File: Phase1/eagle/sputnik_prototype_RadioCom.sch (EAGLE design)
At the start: 73 parts, among them Y1 32MHz

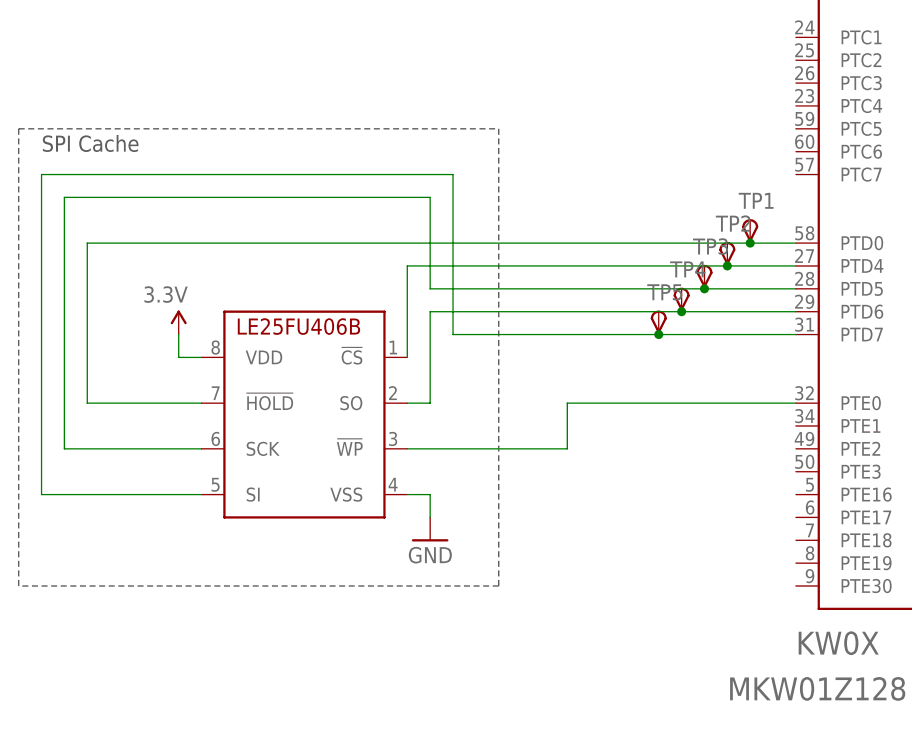
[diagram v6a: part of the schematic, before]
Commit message: Fixed OIs, fixed SysCon LDO, replaced SPI cache
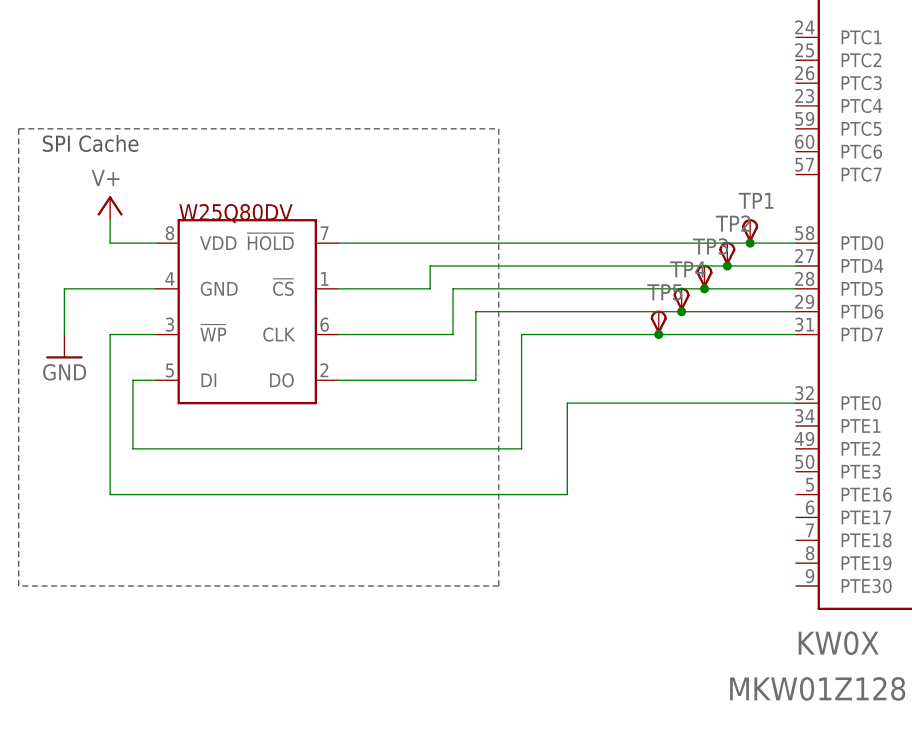
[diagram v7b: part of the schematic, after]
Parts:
- removed CACHE: LE25FU406B, psas_c3_team05:LE25FU406B
- added U$1: W25Q80DV, psas_c3_team05:W25Q80DV
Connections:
- removed net N$4: CACHE.!CS, KW0X.PTD4, TP2.PP
- new net N$28: KW0X.PTD4, TP2.PP, U$1.!CS
- net 3.3V: no longer CACHE.VDD
- net GND: now also U$1.GND; no longer CACHE.VSS
- net N$12: now also U$1.DO; no longer CACHE.SO
- net N$14: now also U$1.CLK; no longer CACHE.SCK
- net N$15: now also U$1.DI; no longer CACHE.SI
- net N$23: now also U$1.!HOLD; no longer CACHE.!HOLD
- net N$26: now also U$1.!WP; no longer CACHE.!WP
- net V+: now also U$1.VDD
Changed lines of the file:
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@@
 <?xml version="1.0" encoding="utf-8"?>
 <!DOCTYPE eagle SYSTEM "eagle.dtd">
-<eagle version="7.3.0">
+<eagle version="7.5.0">
 <drawing>
 <settings>
@@
 <part name="GND41" library="psas_c3_team05" deviceset="GND" device=""/>
 <part name="3.3V2" library="psas_c3_team05" deviceset="V+" device=""/>
-<part name="CACHE" library="psas_c3_team05" deviceset="LE25FU406B" device="">
-<attribute name="DIST" value="Digi-Key"/>
-<attribute name="DPN" value="W25Q80DVSSIG-ND"/>
-<attribute name="MFN" value="Winbond Electronics"/>
-<attribute name="MPN" value="W25Q80DVSSIG"/>
-</part>
 <part name="JP1" library="psas_c3_team05" deviceset="PINHD-1X2" device=""/>
 <part name="GND1" library="psas_c3_team05" deviceset="GND" device=""/>
@@
 <part name="3.3V1" library="psas_c3_team05" deviceset="V+" device=""/>
 <part name="GND34" library="psas_c3_team05" deviceset="GND" device=""/>
-<part name="P+1" library="SparkFun-v5" deviceset="3.3V" device=""/>
 <part name="U$8" library="psas_c3_team05" deviceset="AAT3215" device="">
 <attribute name="MFN" value="Skyworks"/>
@@
 <attribute name="MFN-PN" value="AAT3215"/>
 </part>
+<part name="U$1" library="psas_c3_team05" deviceset="W25Q80DV" device=""/>
+<part name="3.3V4" library="psas_c3_team05" deviceset="V+" device=""/>
 </parts>
 <sheets>
@@
 <instance part="GND41" gate="1" x="452.12" y="304.8"/>
 <instance part="3.3V2" gate="1" x="378.46" y="325.12" rot="MR0"/>
-<instance part="CACHE" gate="G$1" x="48.26" y="177.8" rot="MR0">
-<attribute name="MFN" x="48.26" y="177.8" size="1.778" layer="96" rot="MR0" display="off"/>
-<attribute name="MPN" x="48.26" y="177.8" size="1.778" layer="96" rot="MR0" display="off"/>
-<attribute name="DIST" x="48.26" y="177.8" size="1.778" layer="96" rot="MR0" display="off"/>
-<attribute name="DPN" x="48.26" y="177.8" size="1.778" layer="96" rot="MR0" display="off"/>
-</instance>
 <instance part="JP1" gate="G$1" x="238.76" y="76.2" rot="MR0"/>
 <instance part="GND1" gate="1" x="248.92" y="71.12"/>
@@
 <instance part="C38" gate="CE" x="360.68" y="132.08"/>
 <instance part="3.3V1" gate="1" x="360.68" y="144.78" rot="MR0"/>
-<instance part="GND34" gate="1" x="53.34" y="154.94" rot="MR0"/>
-<instance part="P+1" gate="G$1" x="25.4" y="177.8" rot="MR0"/>
+<instance part="GND34" gate="1" x="12.7" y="175.26" rot="MR0"/>
 <instance part="U$8" gate="G$1" x="55.88" y="307.34">
 <attribute name="MFN" x="55.88" y="307.34" size="1.778" layer="96" display="off"/>
@@
 <attribute name="MFN-PN" x="378.46" y="147.32" size="1.778" layer="96" display="off"/>
 </instance>
+<instance part="U$1" gate="G$1" x="25.4" y="190.5"/>
+<instance part="3.3V4" gate="1" x="17.78" y="193.04" rot="MR0"/>
 </instances>
 <busses>
@@
 </segment>
 <segment>
-<pinref part="GND34" gate="1" pin="GND"/>
-<pinref part="CACHE" gate="G$1" pin="VSS"/>
-<wire x1="53.34" y1="157.48" x2="53.34" y2="160.02" width="0.1524" layer="91"/>
-<wire x1="53.34" y1="160.02" x2="50.8" y2="160.02" width="0.1524" layer="91"/>
-</segment>
-<segment>
 <pinref part="U$8" gate="G$1" pin="GND"/>
 <pinref part="GND35" gate="1" pin="GND"/>
@@
 <junction x="83.82" y="284.48"/>
 </segment>
+<segment>
+<pinref part="U$1" gate="G$1" pin="GND"/>
+<pinref part="GND34" gate="1" pin="GND"/>
+<wire x1="22.86" y1="182.88" x2="12.7" y2="182.88" width="0.1524" layer="91"/>
+<wire x1="12.7" y1="182.88" x2="12.7" y2="177.8" width="0.1524" layer="91"/>
+</segment>
 </net>
 <net name="V+" class="0">
@@
 <pinref part="3.3V3" gate="1" pin="V+"/>
 <junction x="38.1" y="302.26"/>
+</segment>
+<segment>
+<pinref part="U$1" gate="G$1" pin="VDD"/>
+<wire x1="22.86" y1="187.96" x2="17.78" y2="187.96" width="0.1524" layer="91"/>
+<wire x1="17.78" y1="187.96" x2="17.78" y2="190.5" width="0.1524" layer="91"/>
+<pinref part="3.3V4" gate="1" pin="V+"/>
 </segment>
 </net>
@@
 <wire x1="195.58" y1="170.18" x2="181.61" y2="170.18" width="0.1524" layer="91"/>
 <pinref part="P+4" gate="G$1" pin="3.3V"/>
-</segment>
-<segment>
-<pinref part="CACHE" gate="G$1" pin="VDD"/>
-<pinref part="P+1" gate="G$1" pin="3.3V"/>
-<wire x1="27.94" y1="175.26" x2="25.4" y2="175.26" width="0.1524" layer="91"/>
-<wire x1="25.4" y1="175.26" x2="25.4" y2="177.8" width="0.1524" layer="91"/>
 </segment>
 </net>
@@
 </segment>
 </net>
-<net name="N$4" class="0">
-<segment>
-<pinref part="KW0X" gate="G$1" pin="PTD4"/>
-<pinref part="CACHE" gate="G$1" pin="!CS"/>
-<wire x1="93.98" y1="185.42" x2="86.36" y2="185.42" width="0.1524" layer="91"/>
-<wire x1="86.36" y1="185.42" x2="50.8" y2="185.42" width="0.1524" layer="91"/>
-<wire x1="50.8" y1="185.42" x2="50.8" y2="175.26" width="0.1524" layer="91"/>
-<pinref part="TP2" gate="G$1" pin="PP"/>
-<junction x="86.36" y="185.42"/>
-</segment>
-</net>
 <net name="N$12" class="0">
 <segment>
-<pinref part="CACHE" gate="G$1" pin="SO"/>
-<wire x1="50.8" y1="170.18" x2="53.34" y2="170.18" width="0.1524" layer="91"/>
-<wire x1="53.34" y1="170.18" x2="53.34" y2="180.34" width="0.1524" layer="91"/>
+<wire x1="43.18" y1="172.72" x2="58.42" y2="172.72" width="0.1524" layer="91"/>
+<pinref part="U$1" gate="G$1" pin="DO"/>
+<wire x1="58.42" y1="172.72" x2="58.42" y2="180.34" width="0.1524" layer="91"/>
 <pinref part="KW0X" gate="G$1" pin="PTD6"/>
-<wire x1="53.34" y1="180.34" x2="81.28" y2="180.34" width="0.1524" layer="91"/>
 <pinref part="TP4" gate="G$1" pin="PP"/>
 <wire x1="81.28" y1="180.34" x2="93.98" y2="180.34" width="0.1524" layer="91"/>
+<wire x1="58.42" y1="180.34" x2="81.28" y2="180.34" width="0.1524" layer="91"/>
 <junction x="81.28" y="180.34"/>
 </segment>
@@
 <net name="N$14" class="0">
 <segment>
+<wire x1="55.88" y1="177.8" x2="43.18" y2="177.8" width="0.1524" layer="91"/>
+<pinref part="U$1" gate="G$1" pin="CLK"/>
+<wire x1="55.88" y1="177.8" x2="55.88" y2="182.88" width="0.1524" layer="91"/>
 <pinref part="KW0X" gate="G$1" pin="PTD5"/>
 <wire x1="93.98" y1="182.88" x2="83.82" y2="182.88" width="0.1524" layer="91"/>
-<wire x1="83.82" y1="182.88" x2="53.34" y2="182.88" width="0.1524" layer="91"/>
-<wire x1="53.34" y1="182.88" x2="53.34" y2="193.04" width="0.1524" layer="91"/>
-<wire x1="53.34" y1="193.04" x2="12.7" y2="193.04" width="0.1524" layer="91"/>
-<wire x1="12.7" y1="193.04" x2="12.7" y2="165.1" width="0.1524" layer="91"/>
-<pinref part="CACHE" gate="G$1" pin="SCK"/>
-<wire x1="12.7" y1="165.1" x2="27.94" y2="165.1" width="0.1524" layer="91"/>
 <pinref part="TP3" gate="G$1" pin="PP"/>
+<wire x1="55.88" y1="182.88" x2="83.82" y2="182.88" width="0.1524" layer="91"/>
 <junction x="83.82" y="182.88"/>
 </segment>
@@
 <net name="N$15" class="0">
 <segment>
+<wire x1="63.5" y1="165.1" x2="20.32" y2="165.1" width="0.1524" layer="91"/>
+<wire x1="20.32" y1="165.1" x2="20.32" y2="172.72" width="0.1524" layer="91"/>
+<pinref part="U$1" gate="G$1" pin="DI"/>
+<wire x1="20.32" y1="172.72" x2="22.86" y2="172.72" width="0.1524" layer="91"/>
+<wire x1="63.5" y1="165.1" x2="63.5" y2="177.8" width="0.1524" layer="91"/>
 <pinref part="KW0X" gate="G$1" pin="PTD7"/>
 <wire x1="93.98" y1="177.8" x2="78.74" y2="177.8" width="0.1524" layer="91"/>
-<wire x1="78.74" y1="177.8" x2="55.88" y2="177.8" width="0.1524" layer="91"/>
-<wire x1="55.88" y1="177.8" x2="55.88" y2="195.58" width="0.1524" layer="91"/>
-<wire x1="55.88" y1="195.58" x2="10.16" y2="195.58" width="0.1524" layer="91"/>
-<wire x1="10.16" y1="195.58" x2="10.16" y2="160.02" width="0.1524" layer="91"/>
-<pinref part="CACHE" gate="G$1" pin="SI"/>
-<wire x1="10.16" y1="160.02" x2="27.94" y2="160.02" width="0.1524" layer="91"/>
 <pinref part="TP5" gate="G$1" pin="PP"/>
+<wire x1="63.5" y1="177.8" x2="78.74" y2="177.8" width="0.1524" layer="91"/>
 <junction x="78.74" y="177.8"/>
 </segment>
@@
 <pinref part="KW0X" gate="G$1" pin="PTD0"/>
 <wire x1="93.98" y1="187.96" x2="88.9" y2="187.96" width="0.1524" layer="91"/>
-<wire x1="88.9" y1="187.96" x2="15.24" y2="187.96" width="0.1524" layer="91"/>
-<wire x1="15.24" y1="187.96" x2="15.24" y2="170.18" width="0.1524" layer="91"/>
-<pinref part="CACHE" gate="G$1" pin="!HOLD"/>
-<wire x1="15.24" y1="170.18" x2="27.94" y2="170.18" width="0.1524" layer="91"/>
+<wire x1="88.9" y1="187.96" x2="43.18" y2="187.96" width="0.1524" layer="91"/>
 <pinref part="TP1" gate="G$1" pin="PP"/>
 <junction x="88.9" y="187.96"/>
+<pinref part="U$1" gate="G$1" pin="!HOLD"/>
 </segment>
 </net>
 <net name="N$26" class="0">
 <segment>
+<wire x1="68.58" y1="160.02" x2="17.78" y2="160.02" width="0.1524" layer="91"/>
+<wire x1="17.78" y1="160.02" x2="17.78" y2="177.8" width="0.1524" layer="91"/>
+<pinref part="U$1" gate="G$1" pin="!WP"/>
+<wire x1="17.78" y1="177.8" x2="22.86" y2="177.8" width="0.1524" layer="91"/>
 <pinref part="KW0X" gate="G$1" pin="PTE0"/>
 <wire x1="93.98" y1="170.18" x2="68.58" y2="170.18" width="0.1524" layer="91"/>
-<wire x1="68.58" y1="170.18" x2="68.58" y2="165.1" width="0.1524" layer="91"/>
-<pinref part="CACHE" gate="G$1" pin="!WP"/>
-<wire x1="68.58" y1="165.1" x2="50.8" y2="165.1" width="0.1524" layer="91"/>
+<wire x1="68.58" y1="160.02" x2="68.58" y2="170.18" width="0.1524" layer="91"/>
 </segment>
 </net>
@@
 </segment>
 </net>
+<net name="N$28" class="0">
+<segment>
+<pinref part="KW0X" gate="G$1" pin="PTD4"/>
+<wire x1="93.98" y1="185.42" x2="86.36" y2="185.42" width="0.1524" layer="91"/>
+<pinref part="TP2" gate="G$1" pin="PP"/>
+<pinref part="U$1" gate="G$1" pin="!CS"/>
+<wire x1="43.18" y1="182.88" x2="53.34" y2="182.88" width="0.1524" layer="91"/>
+<wire x1="53.34" y1="182.88" x2="53.34" y2="185.42" width="0.1524" layer="91"/>
+<wire x1="53.34" y1="185.42" x2="86.36" y2="185.42" width="0.1524" layer="91"/>
+<junction x="86.36" y="185.42"/>
+</segment>
+</net>

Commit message: Fixed to do list
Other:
- note added: "TODO: -Fix RF GND"
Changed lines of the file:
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@@
 <wire x1="60.96" y1="149.86" x2="7.62" y2="149.86" width="0.1524" layer="97" style="longdash"/>
 <wire x1="7.62" y1="149.86" x2="7.62" y2="200.66" width="0.1524" layer="97" style="longdash"/>
+<text x="99.06" y="116.84" size="1.778" layer="97">TODO:
+-Fix RF GND</text>
 </plain>
 <instances>
